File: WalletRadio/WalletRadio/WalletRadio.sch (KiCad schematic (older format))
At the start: 30 parts, among them Q1001 Q_NMOS_DGS, Q1002 Q_NPN_ECB, SW1001 SW_DIP_x01, U1 LM324A

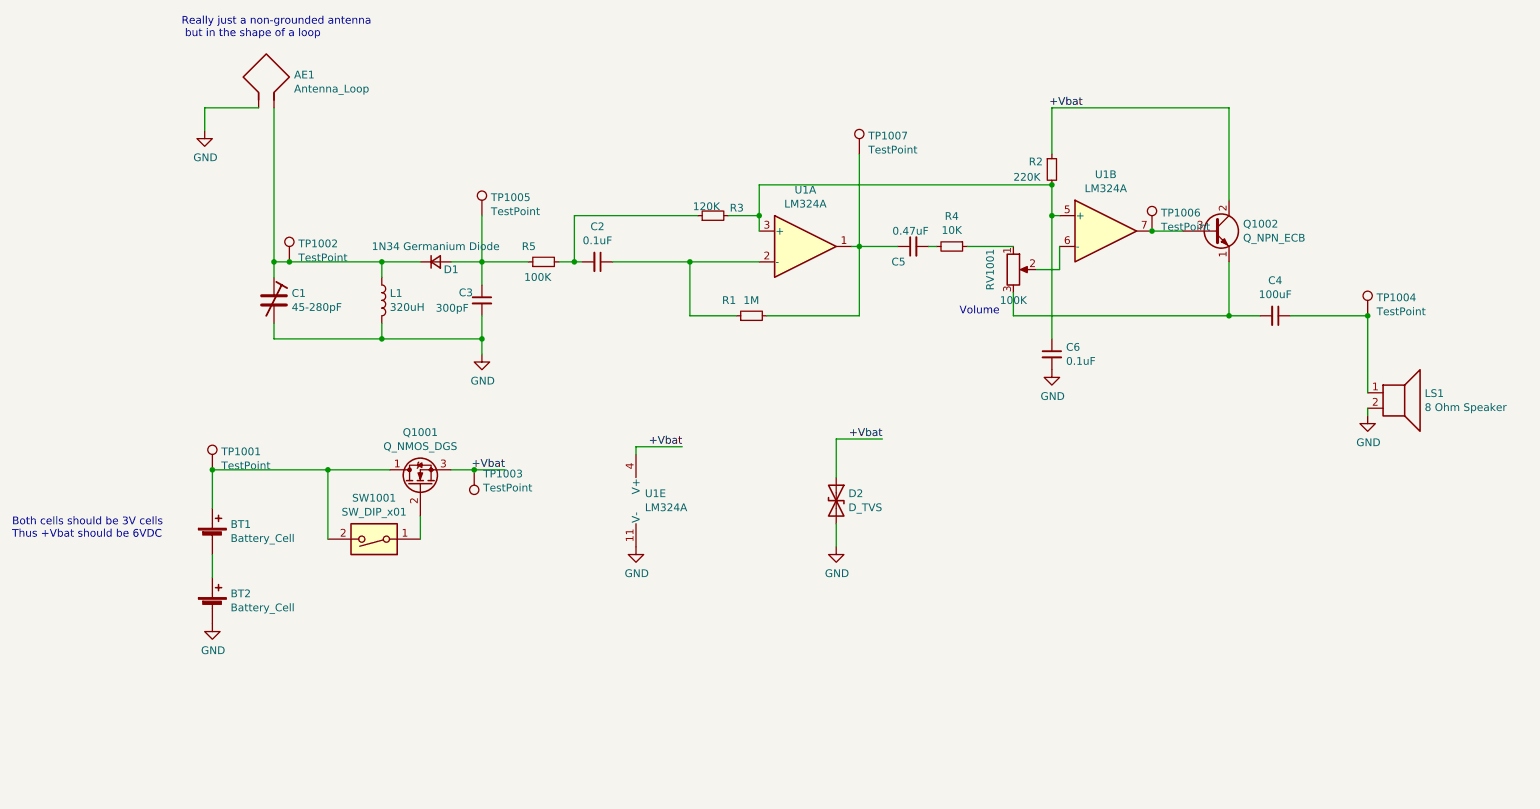
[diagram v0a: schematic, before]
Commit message: Changed the tank circuit to use a varacter diode
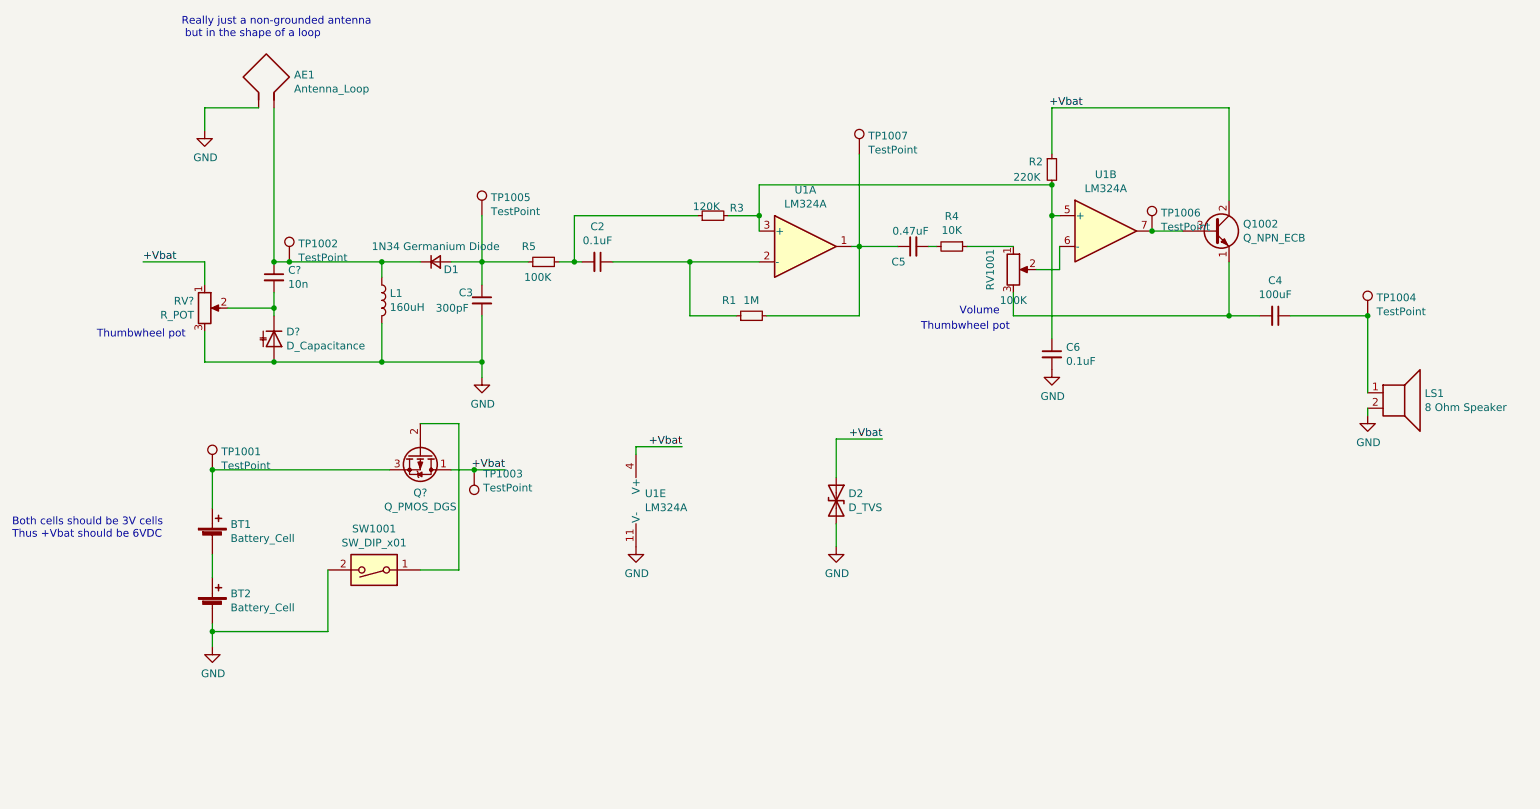
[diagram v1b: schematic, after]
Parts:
- removed C1: 45-280pF, WalletRadio:464-PC_Trimmer, symbol Device:CTRIM
- removed Q1001: Q_NMOS_DGS, Package_TO_SOT_SMD:SOT-23, symbol Device:Q_NMOS_DGS
- added C?: 10n, symbol Device:C_Small
- added D?: D_Capacitance, symbol Device:D_Capacitance
- added Q?: Q_PMOS_DGS, symbol Device:Q_PMOS_DGS
- added RV?: R_POT, symbol Device:R_POT
- L1: value 320uH -> 160uH
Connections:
- net +Vbat: now also Q?.1 (D), RV?.1
- net GND: now also SW1001.2, D?.2 (A), RV?.3
- net at AE1.2, D1.1 (K), L1.1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: now also C?.1
- net at SW1001.1: now also Q?.2 (G)
- net at BT1.1 (+), TP1001.1: now also Q?.3 (S); no longer SW1001.2
- new net: C?.2, D?.1 (K), RV?.2
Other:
- note added: "Thumbwheel pot"
- moved on the sheet: SW1001
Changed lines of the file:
@@
 EESchema Schematic File Version 4
-LIBS:WalletRadio-cache
-EELAYER 29 0
+EELAYER 30 0
 EELAYER END
 $Descr A4 11693 8268
@@
 $EndDescr
 $Comp
-L Device:CTRIM C1
-U 1 1 5EF66DCD
-P 2850 3150
-F 0 "C1" H 2965 3196 50  0000 L CNN
-F 1 "45-280pF" H 2965 3105 50  0000 L CNN
-F 2 "WalletRadio:464-PC_Trimmer" H 2850 3150 50  0001 C CNN
-F 3 "https://www.rfparts.com/464-pc.html" H 2850 3150 50  0001 C CNN
-	1    2850 3150
-	1    0    0    -1
-$EndComp
-$Comp
 L Device:L L1
 U 1 1 5EF68F6A
 P 3550 3150
 F 0 "L1" H 3602 3196 50  0000 L CNN
-F 1 "320uH" H 3602 3105 50  0000 L CNN
+F 1 "160uH" H 3602 3105 50  0000 L CNN
 F 2 "WalletRadio:7447714331_330uH" H 3550 3150 50  0001 C CNN
-F 3 "https://www.digikey.com/product-detail/en/w%C3%BCrth-elektronik/7447714331/732-4111-6-ND/3476554" H 3550 3150 50  0001 C CNN
+F 3 "" H 3550 3150 50  0001 C CNN
 	1    3550 3150
 	1    0    0    -1
@@
 Wire Wire Line
 	2400 1900 2400 2050
-Wire Wire Line
-	4200 3400 4200 3500
 $Comp
 L power:GND #PWR03
 U 1 1 5EF6A910
-P 4200 3500
-F 0 "#PWR03" H 4200 3250 50  0001 C CNN
-F 1 "GND" H 4205 3327 50  0000 C CNN
-F 2 "" H 4200 3500 50  0001 C CNN
-F 3 "" H 4200 3500 50  0001 C CNN
-	1    4200 3500
+P 4200 3650
+F 0 "#PWR03" H 4200 3400 50  0001 C CNN
+F 1 "GND" H 4205 3477 50  0000 C CNN
+F 2 "" H 4200 3650 50  0001 C CNN
+F 3 "" H 4200 3650 50  0001 C CNN
+	1    4200 3650
 	1    0    0    -1
 $EndComp
@@
 Wire Wire Line
 	3550 3000 3550 2900
-Wire Wire Line
-	3550 3300 3550 3400
-Wire Wire Line
-	2850 3300 2850 3400
-Wire Wire Line
-	2850 3000 2850 2900
 $Comp
 L Device:C_Small C3
@@
 $EndComp
 Wire Wire Line
-	4200 3250 4200 3400
-Wire Wire Line
-	4200 3400 3550 3400
-Connection ~ 3550 3400
-Connection ~ 4200 3400
-Wire Wire Line
 	4200 3050 4200 2900
 Wire Wire Line
@@
 	0    -1   -1   0
 $EndComp
-Wire Wire Line
-	2850 3400 3550 3400
 $Comp
 L Device:R_Small R4
@@
 L power:GND #PWR02
 U 1 1 5EFB12B0
-P 2450 5250
-F 0 "#PWR02" H 2450 5000 50  0001 C CNN
-F 1 "GND" H 2455 5077 50  0000 C CNN
-F 2 "" H 2450 5250 50  0001 C CNN
-F 3 "" H 2450 5250 50  0001 C CNN
-	1    2450 5250
+P 2450 5400
+F 0 "#PWR02" H 2450 5150 50  0001 C CNN
+F 1 "GND" H 2455 5227 50  0000 C CNN
+F 2 "" H 2450 5400 50  0001 C CNN
+F 3 "" H 2450 5400 50  0001 C CNN
+	1    2450 5400
 	1    0    0    -1
 $EndComp
@@
 L Switch:SW_DIP_x01 SW1001
 U 1 1 5EF7C51E
-P 3500 4700
-F 0 "SW1001" H 3500 4433 50  0000 C CNN
-F 1 "SW_DIP_x01" H 3500 4524 50  0000 C CNN
-F 2 "WalletRadio:CUS-12TB_Switch" H 3500 4700 50  0001 C CNN
-F 3 "https://www.digikey.com/product-detail/en/nidec-copal-electronics/CUS-12TB/563-1102-1-ND/1124231" H 3500 4700 50  0001 C CNN
-	1    3500 4700
+P 3500 4900
+F 0 "SW1001" H 3500 4633 50  0000 C CNN
+F 1 "SW_DIP_x01" H 3500 4724 50  0000 C CNN
+F 2 "WalletRadio:CUS-12TB_Switch" H 3500 4900 50  0001 C CNN
+F 3 "https://www.digikey.com/product-detail/en/nidec-copal-electronics/CUS-12TB/563-1102-1-ND/1124231" H 3500 4900 50  0001 C CNN
+	1    3500 4900
 	-1   0    0    1
 $EndComp
-$Comp
-L Device:Q_NMOS_DGS Q1001
-U 1 1 5EF886B8
-P 3800 4350
-F 0 "Q1001" V 4143 4350 50  0000 C CNN
-F 1 "Q_NMOS_DGS" V 4052 4350 50  0000 C CNN
-F 2 "Package_TO_SOT_SMD:SOT-23" H 4000 4450 50  0001 C CNN
-F 3 "https://www.diodes.com/assets/Datasheets/DMG3402L.pdf" H 3800 4350 50  0001 C CNN
-	1    3800 4350
-	0    -1   -1   0
-$EndComp
-Wire Wire Line
-	3800 4550 3800 4700
-Wire Wire Line
-	3200 4700 3200 4250
-Wire Wire Line
-	2450 4250 3200 4250
-Wire Wire Line
-	3600 4250 3200 4250
-Connection ~ 3200 4250
 $Comp
 L Device:Q_NPN_ECB Q1002
@@
 	1    0    0    -1
 $EndComp
+Wire Wire Line
+	2850 1900 2850 2900
+$Comp
+L Device:D_Capacitance D?
+U 1 1 61F37861
+P 2850 3400
+F 0 "D?" V 2804 3480 50  0000 L CNN
+F 1 "D_Capacitance" V 2895 3480 50  0000 L CNN
+F 2 "" H 2850 3400 50  0001 C CNN
+F 3 "https://www.nxp.com/docs/en/data-sheet/BB201.pdf" H 2850 3400 50  0001 C CNN
+	1    2850 3400
+	0    1    1    0
+$EndComp
+$Comp
+L Device:R_POT RV?
+U 1 1 61F3CBB0
+P 2400 3200
+F 0 "RV?" H 2331 3246 50  0000 R CNN
+F 1 "R_POT" H 2331 3155 50  0000 R CNN
+F 2 "" H 2400 3200 50  0001 C CNN
+F 3 "~" H 2400 3200 50  0001 C CNN
+	1    2400 3200
+	1    0    0    -1
+$EndComp
+Wire Wire Line
+	4200 3250 4200 3550
+$Comp
+L Device:C_Small C?
+U 1 1 61F47165
+P 2850 3000
+F 0 "C?" H 2942 3046 50  0000 L CNN
+F 1 "10n" H 2942 2955 50  0000 L CNN
+F 2 "" H 2850 3000 50  0001 C CNN
+F 3 "~" H 2850 3000 50  0001 C CNN
+	1    2850 3000
+	1    0    0    -1
+$EndComp
 Connection ~ 2850 2900
 Wire Wire Line
-	2850 1900 2850 2900
+	2850 3100 2850 3200
+Wire Wire Line
+	2850 3550 3550 3550
+Connection ~ 4200 3550
+Wire Wire Line
+	4200 3550 4200 3650
+Wire Wire Line
+	3550 3300 3550 3550
+Connection ~ 3550 3550
+Wire Wire Line
+	3550 3550 4200 3550
+Wire Wire Line
+	2550 3200 2850 3200
+Connection ~ 2850 3200
+Wire Wire Line
+	2850 3200 2850 3250
+Wire Wire Line
+	2400 3350 2400 3550
+Wire Wire Line
+	2400 3550 2850 3550
+Connection ~ 2850 3550
+Text Label 2000 2900 0    50   ~ 0
++Vbat
+Wire Wire Line
+	2400 2900 2400 3050
+Wire Wire Line
+	2000 2900 2400 2900
+$Comp
+L Device:Q_PMOS_DGS Q?
+U 1 1 61F5BA5E
+P 3800 4150
+F 0 "Q?" V 4049 4150 50  0000 C CNN
+F 1 "Q_PMOS_DGS" V 4140 4150 50  0000 C CNN
+F 2 "" H 4000 4250 50  0001 C CNN
+F 3 "~" H 3800 4150 50  0001 C CNN
+	1    3800 4150
+	0    1    1    0
+$EndComp
+Wire Wire Line
+	2450 4250 3600 4250
+Wire Wire Line
+	4050 3950 3800 3950
+Wire Wire Line
+	4050 3950 4050 4900
+Wire Wire Line
+	4050 4900 3800 4900
+Wire Wire Line
+	2450 5250 2450 5300
+Wire Wire Line
+	2450 5300 3200 5300
+Wire Wire Line
+	3200 5300 3200 4900
+Connection ~ 2450 5300
+Wire Wire Line
+	2450 5300 2450 5400
+Text Notes 7050 3350 0    50   ~ 0
+Thumbwheel pot
+Text Notes 1700 3400 0    50   ~ 0
+Thumbwheel pot
 $EndSCHEMATC

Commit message: Swapped out several parts and did some rerouting
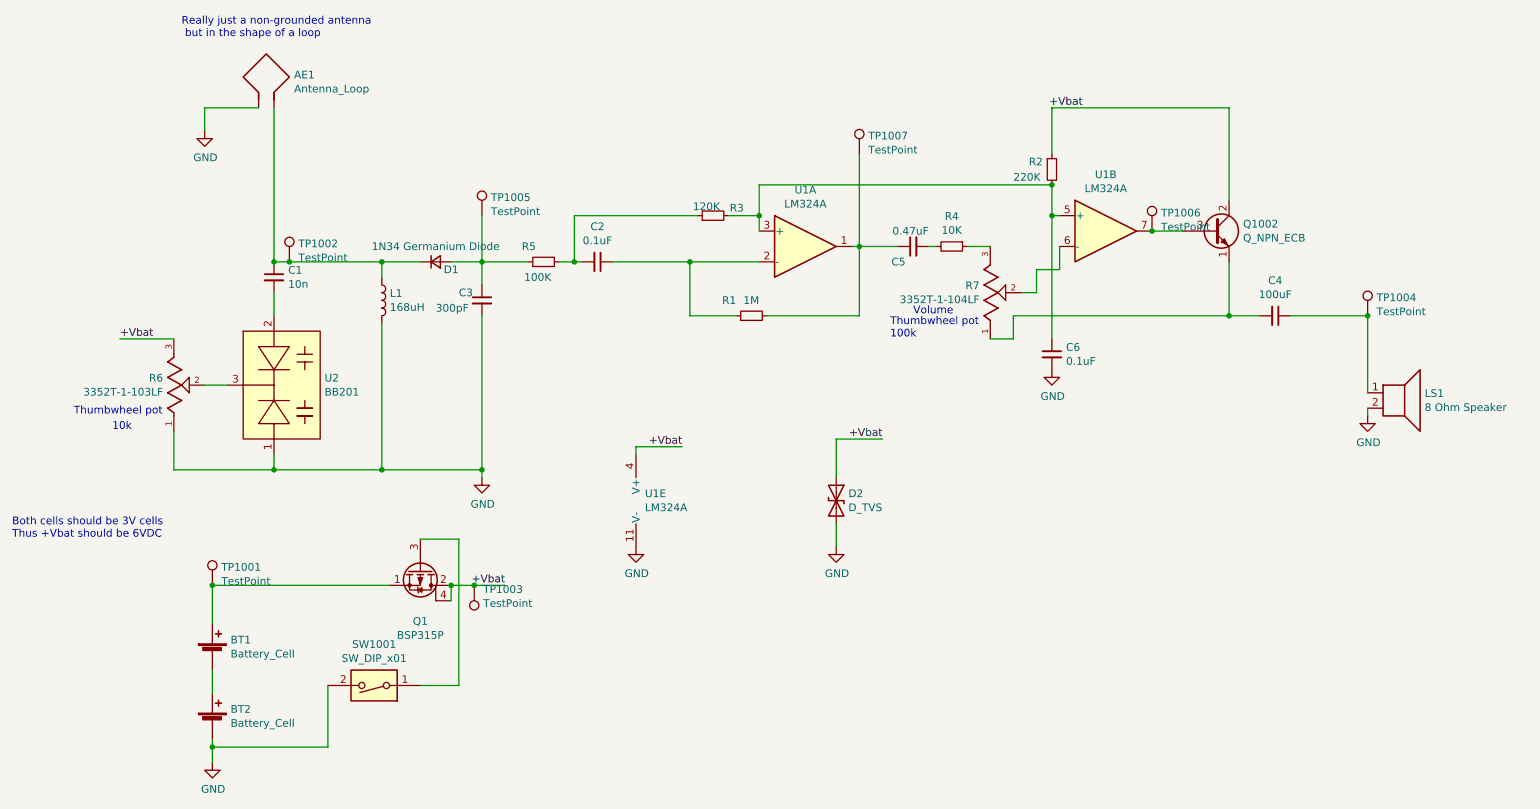
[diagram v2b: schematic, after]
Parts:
- removed D?: D_Capacitance, symbol Device:D_Capacitance
- removed Q?: Q_PMOS_DGS, symbol Device:Q_PMOS_DGS
- removed RV1001: 100K, WalletRadio:100Ohm_Pot, symbol Device:R_POT
- removed RV?: R_POT, symbol Device:R_POT
- added Q1: BSP315P, Package_TO_SOT_SMD:SOT-223, symbol Device:Q_PMOS_SDGD
- added R6: 3352T-1-103LF, WalletRadio:TRIM_3352T-1-103LF, symbol 3352T-1-103LF:3352T-1-103LF
- added R7: 3352T-1-104LF, WalletRadio:TRIM_3352T-1-103LF, symbol 3352T-1-103LF:3352T-1-103LF
- added U2: BB201, Package_TO_SOT_SMD:SOT-23_Handsoldering, symbol WalletRadioLib:BB201
- C1: renamed from C?; footprint (none) -> Capacitor_SMD:C_0603_1608Metric_Pad1.08x0.95mm_HandSolder
- L1: value 160uH -> 168uH; footprint WalletRadio:7447714331_330uH -> WalletRadio:PE-53828NL
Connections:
- net +Vbat: now also Q1.2 (D), Q1.4 (D), R6.3
- net GND: now also R6.1, U2.1
- net at R4.1: now also R7.3
- net at SW1001.1: now also Q1.3 (G)
- net at U1.6 (-): now also R7.2
- net at C4.2, Q1002.1 (E): now also R7.1
- net at BT1.1 (+), TP1001.1: now also Q1.1 (S)
- net at C1.2: now also U2.2
- new net: R6.2, U2.3
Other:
- note added: "10k\n"
- note added: "Thumbwheel pot\n100k"
- moved on the sheet: BT1, BT2, SW1001, TP1001, TP1003
